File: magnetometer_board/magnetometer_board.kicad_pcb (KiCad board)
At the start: 2 copper layers, 11.7 x 21.8 mm, 12 parts, among them J2 S4B-PH-K-S_LF__SN_, U1 MLX90393SLW-ABA-011-RE, U2 MLX90393SLW-ABA-011-RE, U3 MLX90393SLW-ABA-011-RE

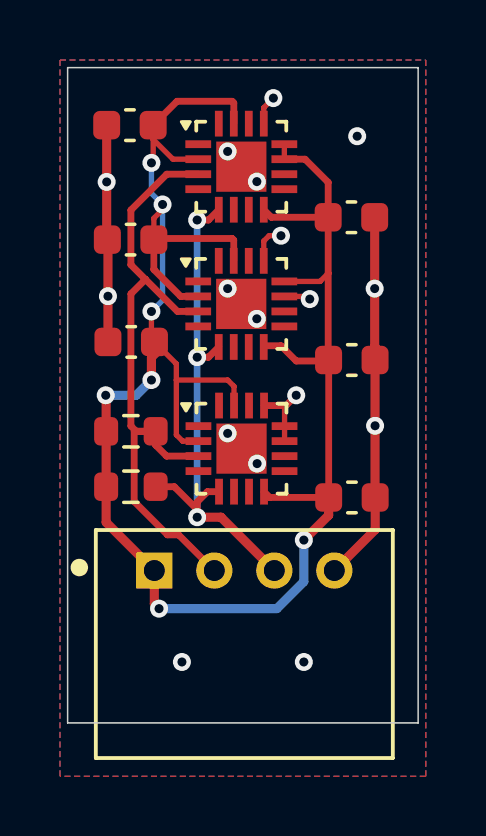
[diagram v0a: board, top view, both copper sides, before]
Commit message: Fixed actuator board and revised magnetometer board
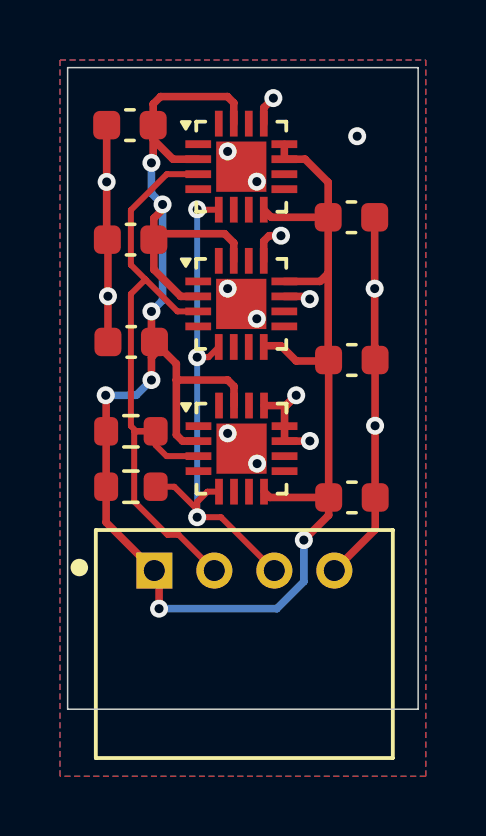
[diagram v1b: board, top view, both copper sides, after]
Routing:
- net GND: track 29.9 -> 30.8 mm, vias 17 -> 16
- net +3V3: track 68.1 -> 68.8 mm
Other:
- board size 11.7 x 21.8 mm -> 11.7 x 21.4 mm

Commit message: updates
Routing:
- net +3V3: track 68.8 -> 69.0 mm, vias 7 -> 5
- net GND: track 30.8 -> 30.7 mm, vias 16 -> 17

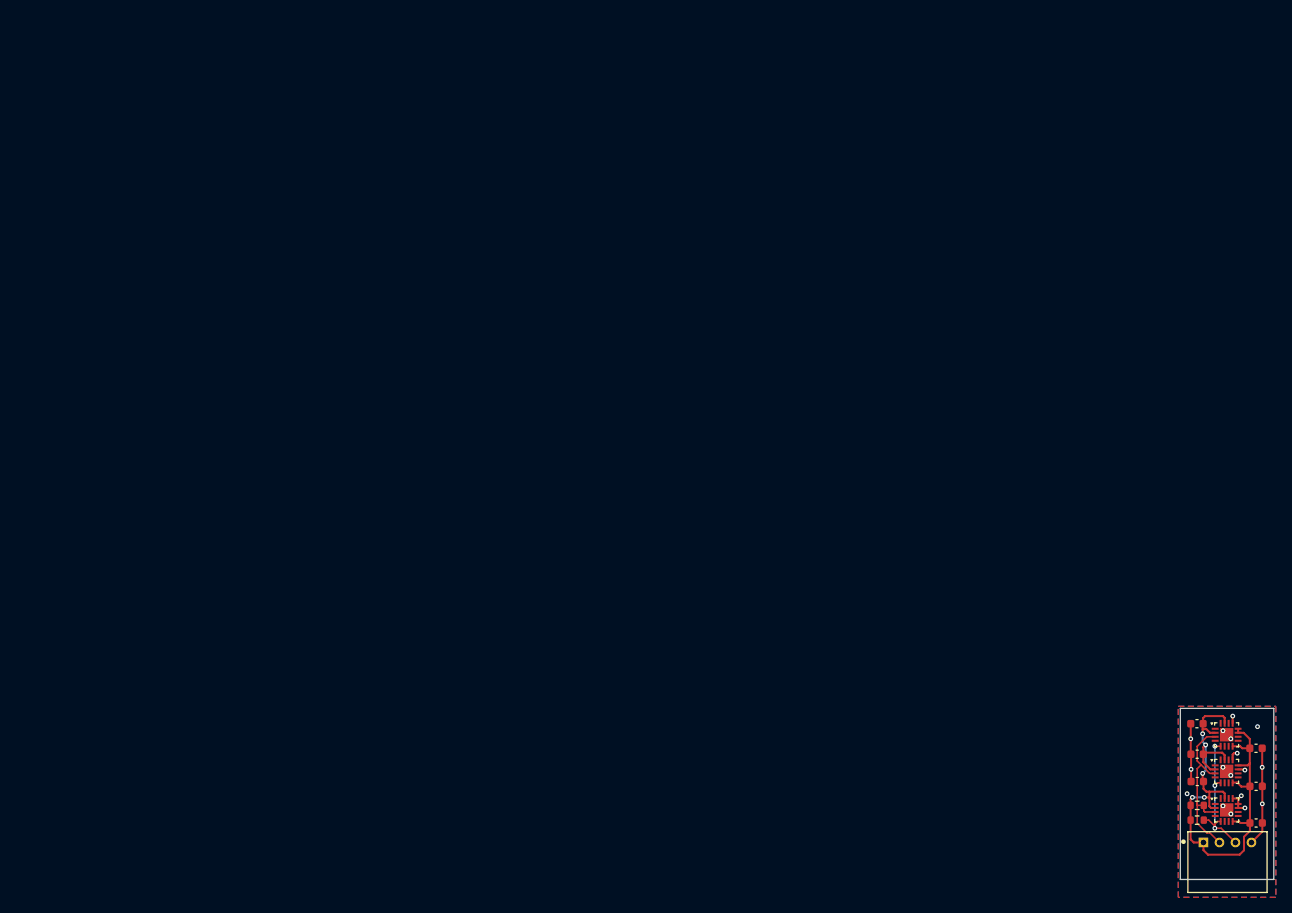
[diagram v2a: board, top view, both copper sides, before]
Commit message: Fixed battery issues, removed LDOs
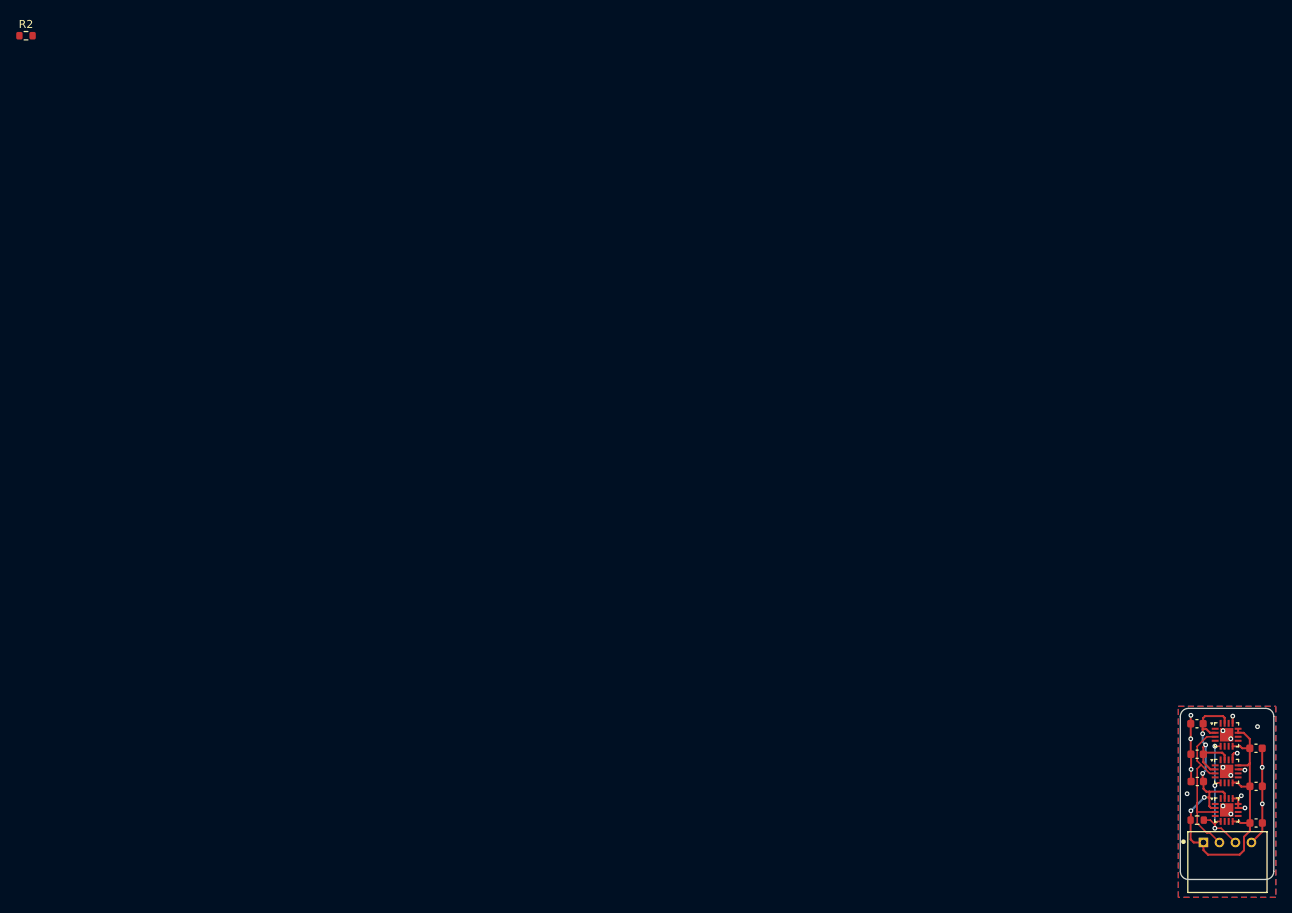
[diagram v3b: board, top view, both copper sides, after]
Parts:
- moved R2 175.2 mm to (1.50, 0.76)
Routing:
- net GND: track 30.7 -> 31.8 mm, vias 17 -> 18
- net +3V3: track 69.0 -> 68.1 mm
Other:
- outline, holes or cut-outs redrawn

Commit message: Final version
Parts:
- removed R2: 10k, Resistor_SMD:R_0603_1608Metric
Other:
- outline, holes or cut-outs redrawn
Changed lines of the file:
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@@
+			)
+		)
+		(model "${KIPRJMOD}/S4B-PH-K-S_LF__SN_/S4B-PH-K-S_LF__SN_.step"
+			(offset
+				(xyz -2.032 1.27 0)
+			)
+			(scale
+				(xyz 1 1 1)
+			)
+			(rotate
+				(xyz -90 -0 -0)
 			)
 		)
@@
 		)
 		(embedded_fonts no)
-		(model "/Users/akshay/Desktop/classes/magnetometer_board/MLX90393SLW_ABA_011_RE/MLX90393SLWABA011RE.STEP"
+		(model "${KIPRJMOD}/MLX90393SLW_ABA_011_RE/MLX90393SLWABA011RE.STEP"
 			(offset
 				(xyz 0 0 0)
@@
 		)
 		(embedded_fonts no)
-		(model "/Users/akshay/Desktop/classes/magnetometer_board/MLX90393SLW_ABA_011_RE/MLX90393SLWABA011RE.STEP"
+		(model "${KIPRJMOD}/MLX90393SLW_ABA_011_RE/MLX90393SLWABA011RE.STEP"
 			(offset
 				(xyz 0 0 0)
@@
 		)
 	)
-	(footprint "Resistor_SMD:R_0603_1608Metric"
-		(layer "F.Cu")
-		(at 1.505 0.755)
-		(descr "Resistor SMD 0603 (1608 Metric), square (rectangular) end terminal, IPC_7351 nominal, (Body size source: IPC-SM-782 page 72, https://www.pcb-3d.com/wordpress/wp-content/uploads/ipc-sm-782a_amendment_1_and_2.pdf), generated with kicad-footprint-generator")
-		(tags "resistor")
-		(property "Reference" "R2"
-			(at 0 -1.43 0)
-			(layer "F.SilkS")
-			(effects
-				(font
-					(size 1 1)
-					(thickness 0.15)
-				)
-			)
-		)
-		(property "Value" "10k"
-			(at 0 1.43 0)
-			(layer "F.Fab")
-			(effects
-				(font
-					(size 1 1)
-					(thickness 0.15)
-				)
-			)
-		)
-		(property "Datasheet" ""
-			(at 0 0 0)
-			(unlocked yes)
-			(layer "F.Fab")
-			(hide yes)
-			(effects
-				(font
-					(size 1.27 1.27)
-					(thickness 0.15)
-				)
-			)
-		)
-		(property "Description" "Resistor, US symbol"
-			(at 0 0 0)
-			(unlocked yes)
-			(layer "F.Fab")
-			(hide yes)
-			(effects
-				(font
-					(size 1.27 1.27)
-					(thickness 0.15)
-				)
-			)
-		)
-		(property ki_fp_filters "R_*")
-		(sheetname "/")
-		(sheetfile "magnetometer_board.kicad_sch")
-		(attr smd)
-		(fp_line
-			(start -0.237258 -0.5225)
-			(end 0.237258 -0.5225)
-			(stroke
-				(width 0.12)
-				(type solid)
-			)
-			(layer "F.SilkS")
-		)
-		(fp_line
-			(start -0.237258 0.5225)
-			(end 0.237258 0.5225)
-			(stroke
-				(width 0.12)
-				(type solid)
-			)
-			(layer "F.SilkS")
-		)
-		(fp_line
-			(start -1.48 -0.73)
-			(end 1.48 -0.73)
-			(stroke
-				(width 0.05)
-				(type solid)
-			)
-			(layer "F.CrtYd")
-		)
-		(fp_line
-			(start -1.48 0.73)
-			(end -1.48 -0.73)
-			(stroke
-				(width 0.05)
-				(type solid)
-			)
-			(layer "F.CrtYd")
-		)
-		(fp_line
-			(start 1.48 -0.73)
-			(end 1.48 0.73)
-			(stroke
-				(width 0.05)
-				(type solid)
-			)
-			(layer "F.CrtYd")
-		)
-		(fp_line
-			(start 1.48 0.73)
-			(end -1.48 0.73)
-			(stroke
-				(width 0.05)
-				(type solid)
-			)
-			(layer "F.CrtYd")
-		)
-		(fp_line
-			(start -0.8 -0.4125)
-			(end 0.8 -0.4125)
-			(stroke
-				(width 0.1)
-				(type solid)
-			)
-			(layer "F.Fab")
-		)
-		(fp_line
-			(start -0.8 0.4125)
-			(end -0.8 -0.4125)
-			(stroke
-				(width 0.1)
-				(type solid)
-			)
-			(layer "F.Fab")
-		)
-		(fp_line
-			(start 0.8 -0.4125)
-			(end 0.8 0.4125)
-			(stroke
-				(width 0.1)
-				(type solid)
-			)
-			(layer "F.Fab")
-		)
-		(fp_line
-			(start 0.8 0.4125)
-			(end -0.8 0.4125)
-			(stroke
-				(width 0.1)
-				(type solid)
-			)
-			(layer "F.Fab")
-		)
-		(fp_text user "${REFERENCE}"
-			(at 0 0 0)
-			(layer "F.Fab")
-			(effects
-				(font
-					(size 0.4 0.4)
-					(thickness 0.06)
-				)
-			)
-		)
-		(pad "1" smd roundrect
-			(at -0.825 0)
-			(size 0.8 0.95)
-			(layers "F.Cu" "F.Mask" "F.Paste")
-			(roundrect_rratio 0.25)
-			(net 2 "+3V3")
-			(pintype "passive")
-		)
-		(pad "2" smd roundrect
-			(at 0.825 0)
-			(size 0.8 0.95)
-			(layers "F.Cu" "F.Mask" "F.Paste")
-			(roundrect_rratio 0.25)
-			(net 3 "/SCL")
-			(pintype "passive")
-		)
-		(embedded_fonts no)
-		(model "${KICAD9_3DMODEL_DIR}/Resistor_SMD.3dshapes/R_0603_1608Metric.wrl"
-			(offset
-				(xyz 0 0 0)
-			)
-			(scale
-				(xyz 1 1 1)
-			)
-			(rotate
-				(xyz 0 0 0)
-			)
-		)
-	)
 	(footprint "Capacitor_SMD:C_0603_1608Metric"
 		(layer "F.Cu")
@@
 		)
 		(embedded_fonts no)
-		(model "/Users/akshay/Desktop/classes/magnetometer_board/MLX90393SLW_ABA_011_RE/MLX90393SLWABA011RE.STEP"
+		(model "${KIPRJMOD}/MLX90393SLW_ABA_011_RE/MLX90393SLWABA011RE.STEP"
 			(offset
 				(xyz 0 0 0)
@@
 		)
 	)
-	(gr_arc
-		(start 157.48 105.2068)
-		(mid 157.18242 105.92522)
-		(end 156.464 106.2228)
+	(gr_line
+		(start 157.48 86.36)
+		(end 157.48 104.7242)
 		(stroke
 			(width 0.05)
@@
 	)
 	(gr_arc
-		(start 145.796 85.852)
-		(mid 146.09358 85.13358)
-		(end 146.812 84.836)
+		(start 147.2946 106.2482)
+		(mid 146.216969 105.801831)
+		(end 145.7706 104.7242)
 		(stroke
 			(width 0.05)
@@
 	)
 	(gr_line
-		(start 146.812 84.836)
-		(end 156.464 84.836)
+		(start 145.7706 104.7242)
+		(end 145.7706 86.36)
 		(stroke
 			(width 0.05)
@@
 		(layer "Edge.Cuts")
 	)
-	(gr_line
-		(start 156.464 106.2228)
-		(end 146.812 106.2228)
+	(gr_arc
+		(start 145.7706 86.36)
+		(mid 146.216969 85.282369)
+		(end 147.2946 84.836)
 		(stroke
 			(width 0.05)
@@
 		(layer "Edge.Cuts")
 	)
-	(gr_line
-		(start 157.48 85.852)
-		(end 157.48 105.2068)
+	(gr_arc
+		(start 157.48 104.7242)
+		(mid 157.033631 105.801831)
+		(end 155.956 106.2482)
 		(stroke
 			(width 0.05)
@@
 	)
 	(gr_line
-		(start 145.796 105.2068)
-		(end 145.796 85.852)
+		(start 155.956 106.2482)
+		(end 147.2946 106.2482)
 		(stroke
 			(width 0.05)
@@
 	)
 	(gr_arc
-		(start 146.812 106.2228)
-		(mid 146.09358 105.92522)
-		(end 145.796 105.2068)
+		(start 155.956 84.836)
+		(mid 157.033631 85.282369)
+		(end 157.48 86.36)
 		(stroke
 			(width 0.05)
@@
 		(layer "Edge.Cuts")
 	)
-	(gr_arc
-		(start 156.464 84.836)
-		(mid 157.18242 85.13358)
-		(end 157.48 85.852)
+	(gr_line
+		(start 147.2946 84.836)
+		(end 155.956 84.836)
 		(stroke
 			(width 0.05)
